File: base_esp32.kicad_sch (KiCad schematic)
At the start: 73 parts, among them J1 Input Source, J10 H_IO15_OUT, J11 H_IO32_OUT, J12 H_IO02_OUT, J13 H_IO04_OUT, J14 5V, J15 5V, J16 H_3V3_1, J17 H_IO34, J18 H_IO35, J19 H_IO36, J2 BYPASS_SRC_5V, J20 H_IO39, J21 S_3V3_1, J22 H_3V3_2, J23 H_KEYPAD, J24 H_I2C, J25 H_SPI, J26 TX_RX, J27 S_3V3_2, J28 H_GND, J29 S_KEYPAD, J3 BYPASS_SRC_3V3, J30 S_I2C, J31 S_SPI, J32 S_GND, J33 Src Board, J4 H_IO33, J5 H_IO15, J6 H_IO32, J7 H_IO02, J8 H_IO04, J9 H_IO33_OUT, SW1 INPUT_D1, SW2 INPUT_D2, SW3 SW_DIP_INPUTS, SW4 ENABLE, SW5 SW_DIP_KEYPAD, SW6 Selector_Input, SW7 Selector_Input, SW8 BOOT, U1 LM7805_TO220, U2 AMS1117, U3 AMS1117, U4 ESP32-DevKitC

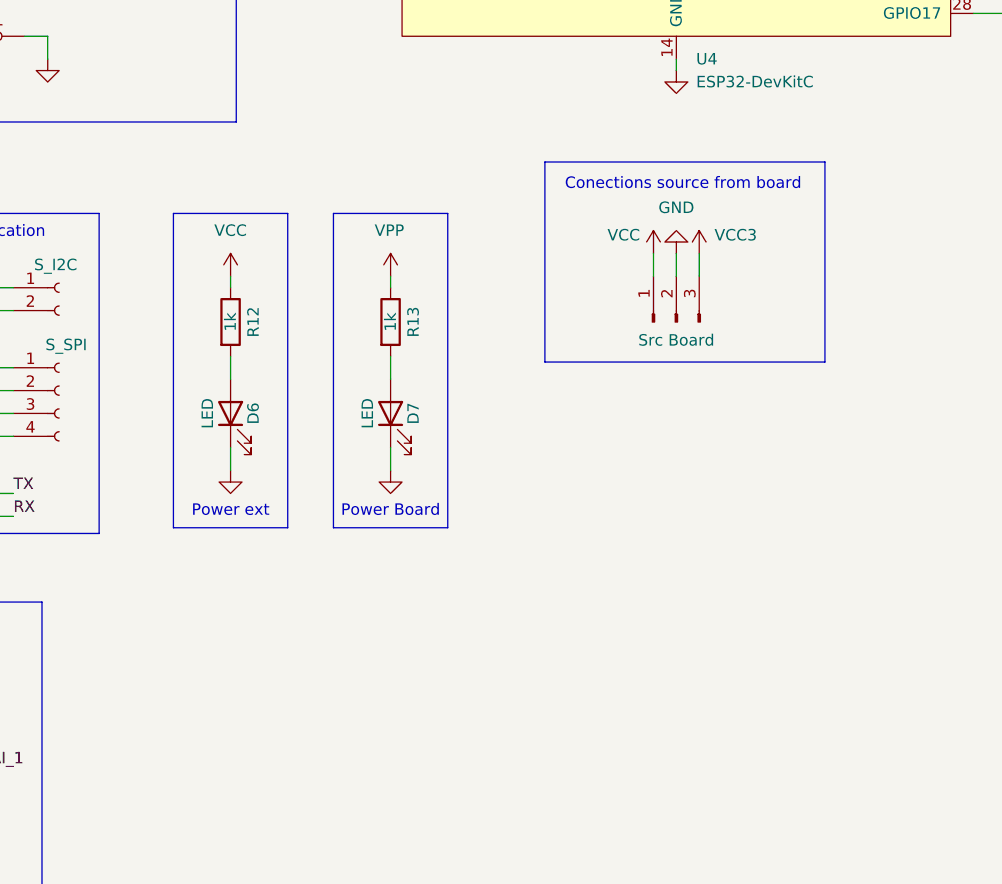
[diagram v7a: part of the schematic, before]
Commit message: add: mounting holes
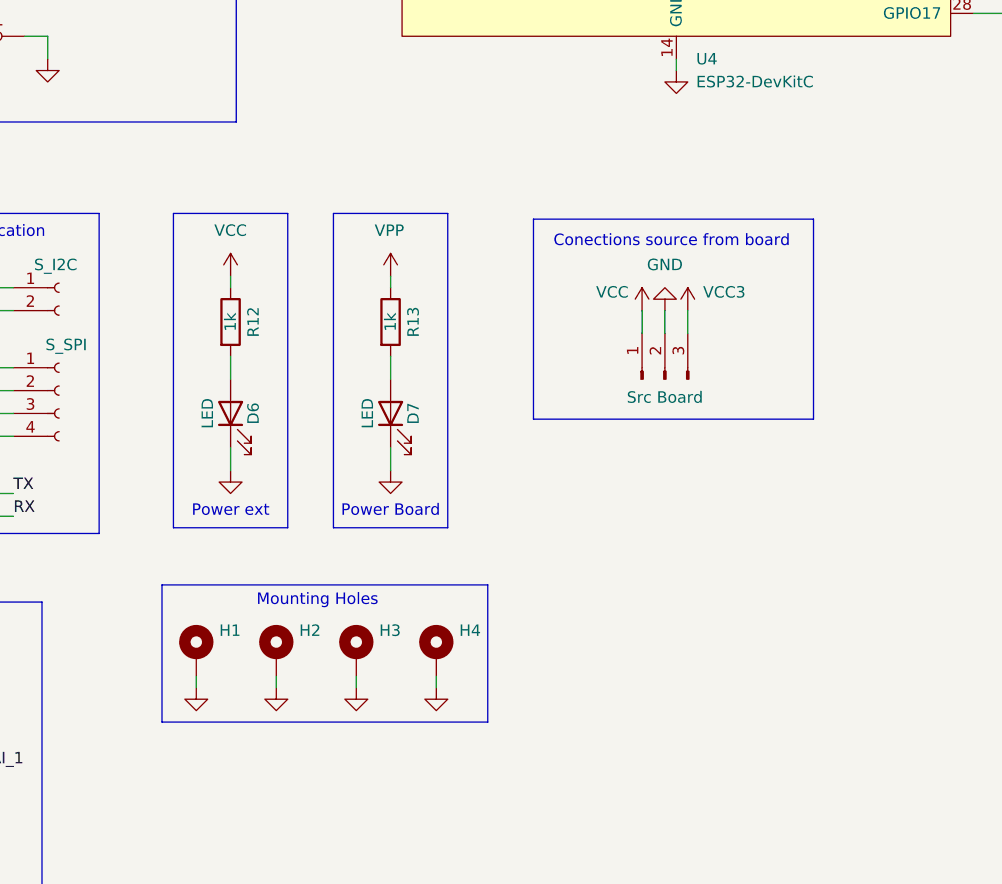
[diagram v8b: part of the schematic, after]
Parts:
- added H1, H2, H3, H4: MountingHole_Pad, MountingHole:MountingHole_3mm_Pad_TopBottom, symbol Mechanical:MountingHole_Pad
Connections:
- net GND: now also H1.1, H2.1, H3.1, H4.1
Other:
- note added: "Mounting Holes"
